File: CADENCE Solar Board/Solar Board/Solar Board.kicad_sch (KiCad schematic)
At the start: 52 parts, among them J1 Conn_01x08, U1 INA230AIRGTT, U2 AD7414ARTZ-1REEL7, U3 OPT3001IDNPRQ1

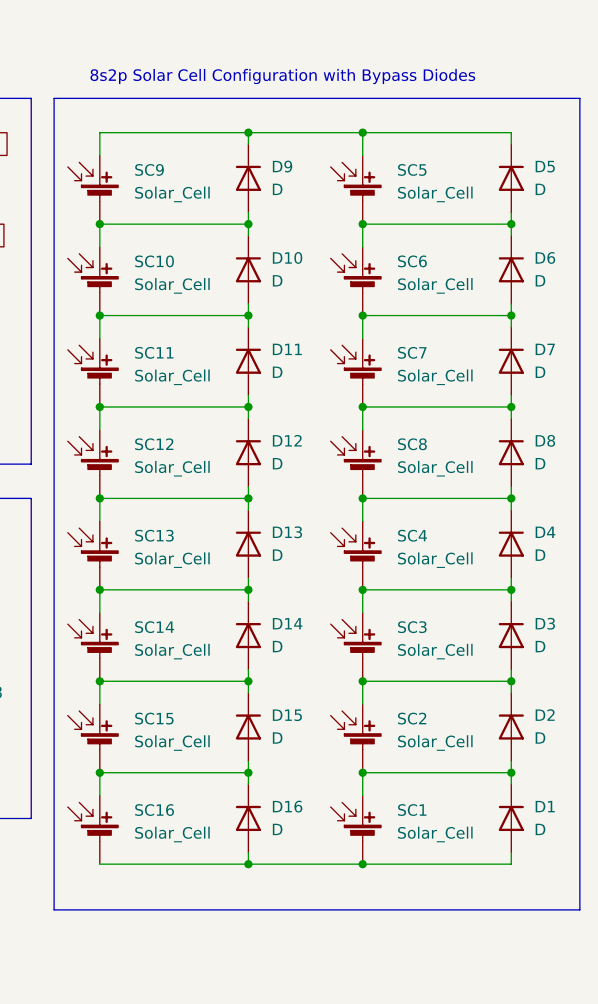
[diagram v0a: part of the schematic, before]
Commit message: added basic PCB layout and attached footprints to parts (excluding solar cells. a lot might need updating later)
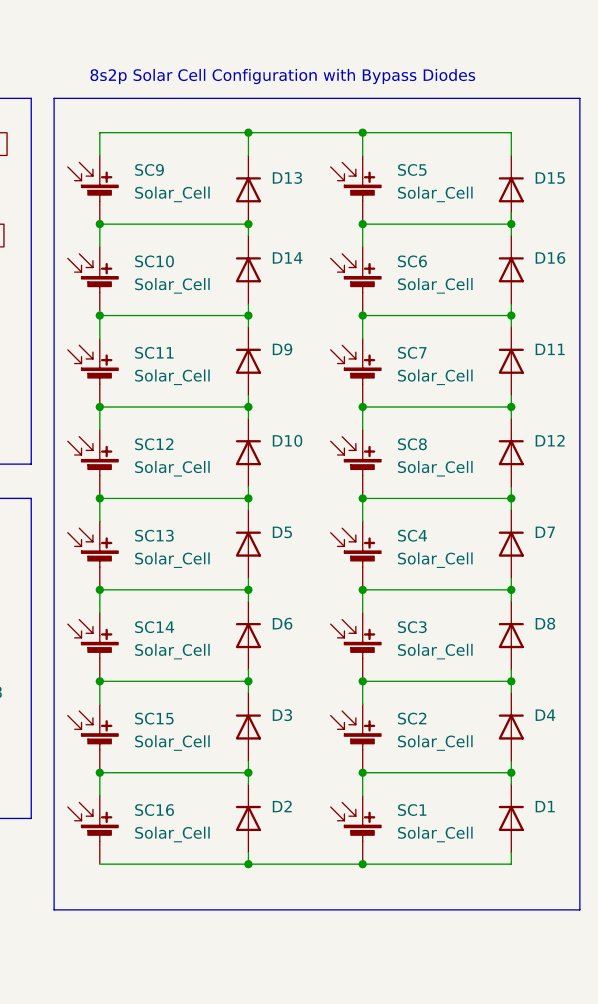
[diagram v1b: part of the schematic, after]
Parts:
- D1, D10, D11, D12, D13, D14, D15, D16, D2, D3, D4, D5, D6, D7, D8, D9: footprint (none) -> Diode_SMD:D_01005_0402Metric
- J1: footprint (none) -> Connector_PinHeader_1.00mm:PinHeader_1x08_P1.00mm_Horizontal
- R1, R10, R2, R3, R4, R5, R6, R7, R8, R9: footprint (none) -> Resistor_SMD:R_01005_0402Metric
- TP1, TP2, TP3: footprint (none) -> Connector_Pin:Pin_D1.3mm_L11.0mm_LooseFit
- U1: footprint QFN50P300X300X100-17N-D -> INA230AIRGTT:QFN50P300X300X100-17N-D
- U2: footprint SOT95P280X145-6N -> AD7414ARTZ-1REEL7:SOT95P280X145-6N
- U3: footprint SON65P200X200X65-7N-D -> OPT3001IDNPRQ1:SON65P200X200X65-7N-D
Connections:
- net at SC10.1 (+), SC9.2 (-): now also D13.2 (A), D14.1 (K); no longer D10.1 (K), D9.2 (A)
- net at SC10.2 (-), SC11.1 (+): now also D14.2 (A), D9.1 (K); no longer D10.2 (A), D11.1 (K)
- net at SC11.2 (-), SC12.1 (+): now also D10.1 (K), D9.2 (A); no longer D11.2 (A), D12.1 (K)
- net at SC12.2 (-), SC13.1 (+): now also D10.2 (A), D5.1 (K); no longer D12.2 (A), D13.1 (K)
- net at SC5.1 (+), SC9.1 (+): now also D13.1 (K), D15.1 (K); no longer D5.1 (K), D9.1 (K)
- net at SC6.2 (-), SC7.1 (+): now also D11.1 (K), D16.2 (A); no longer D6.2 (A), D7.1 (K)
- net at D7.2 (A), D8.1 (K): now also SC3.1 (+), SC4.2 (-); no longer SC7.2 (-), SC8.1 (+)
- net at SC13.2 (-), SC14.1 (+): now also D5.2 (A), D6.1 (K); no longer D13.2 (A), D14.1 (K)
- net at D1.1 (K), SC1.1 (+), SC2.2 (-): now also D4.2 (A); no longer D2.2 (A)
- net at D1.2 (A), SC1.2 (-), SC16.2 (-): now also D2.2 (A); no longer D16.2 (A)
- net at SC14.2 (-), SC15.1 (+): now also D3.1 (K), D6.2 (A); no longer D14.2 (A), D15.1 (K)
- net at SC15.2 (-), SC16.1 (+): now also D2.1 (K), D3.2 (A); no longer D15.2 (A), D16.1 (K)
- net at SC4.1 (+), SC8.2 (-): now also D12.2 (A), D7.1 (K); no longer D4.1 (K), D8.2 (A)
- net at SC2.1 (+), SC3.2 (-): now also D4.1 (K), D8.2 (A); no longer D2.1 (K), D3.2 (A)
- net at SC5.2 (-), SC6.1 (+): now also D15.2 (A), D16.1 (K); no longer D5.2 (A), D6.1 (K)
- new net: D11.2 (A), D12.1 (K), SC7.2 (-), SC8.1 (+)

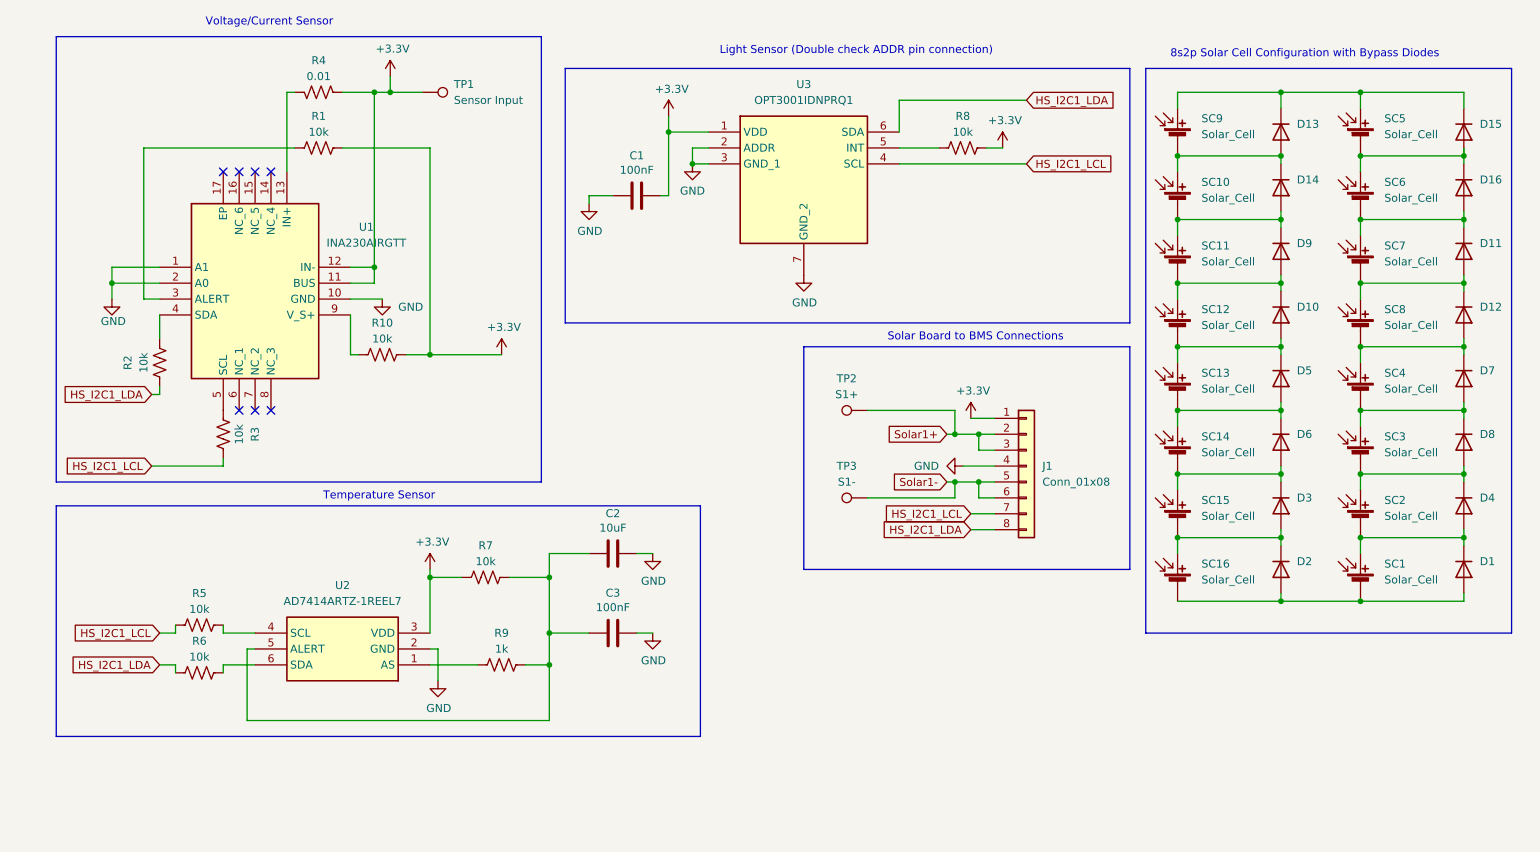
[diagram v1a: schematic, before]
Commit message: corrected board based on octavio's review
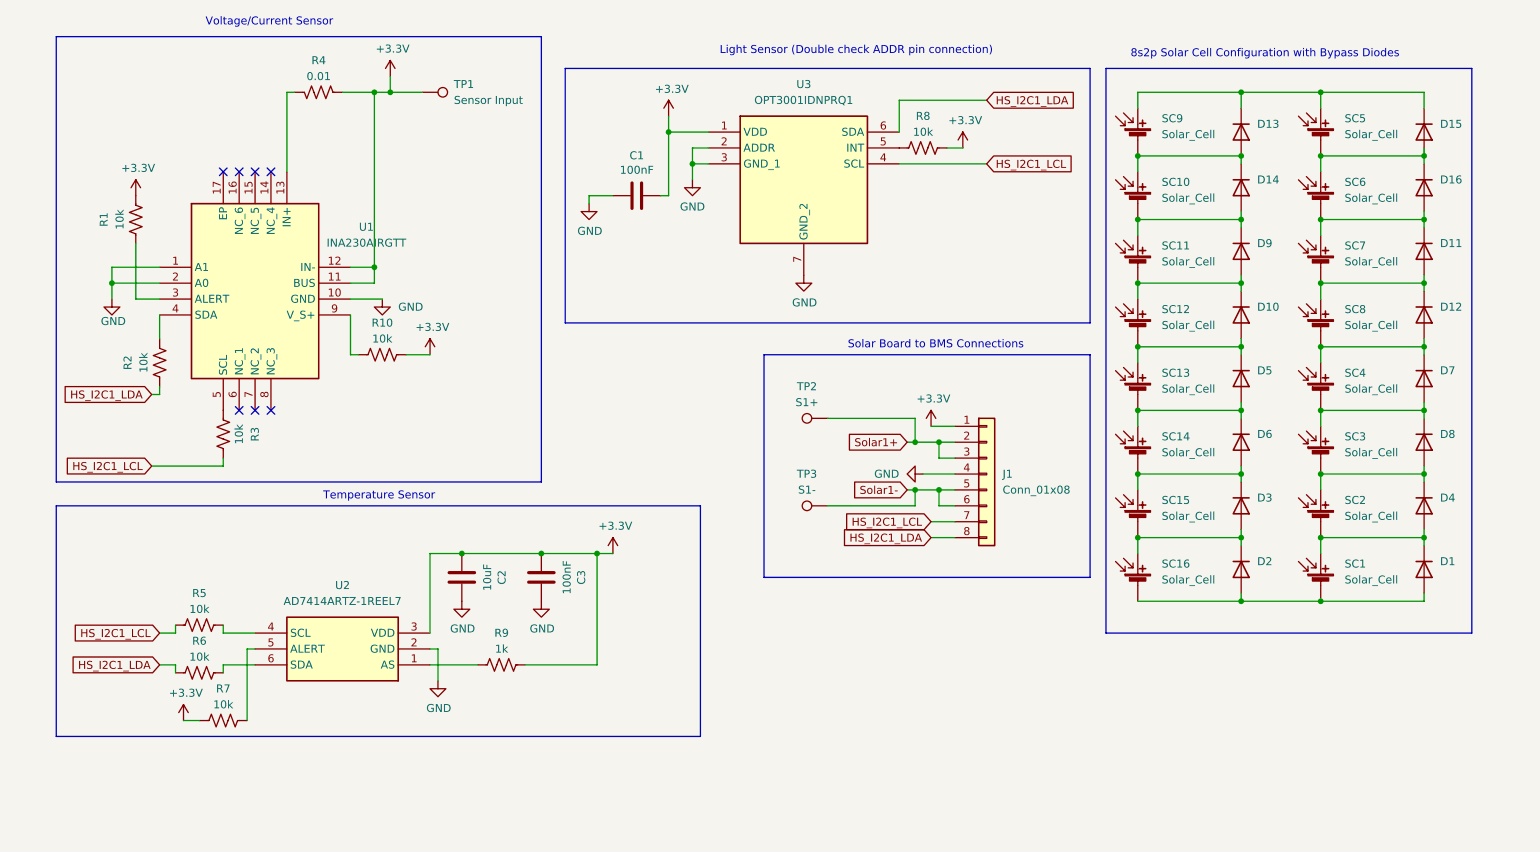
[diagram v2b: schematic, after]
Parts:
- R7: footprint Resistor_SMD:R_01005_0402Metric -> (none)
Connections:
- net +3.3V: now also C2.1, C3.1, R9.2
- new net: R7.2, U2.5 (ALERT)
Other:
- moved on the sheet: C2, C3, D1, D10, D11, D12, D13, D14, D15, D16, D2, D3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

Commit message: corrected board based on octavio's review
added led with resistor to ALERT pins, removed extra resistors, biased high configuration for the voltage/current sensor
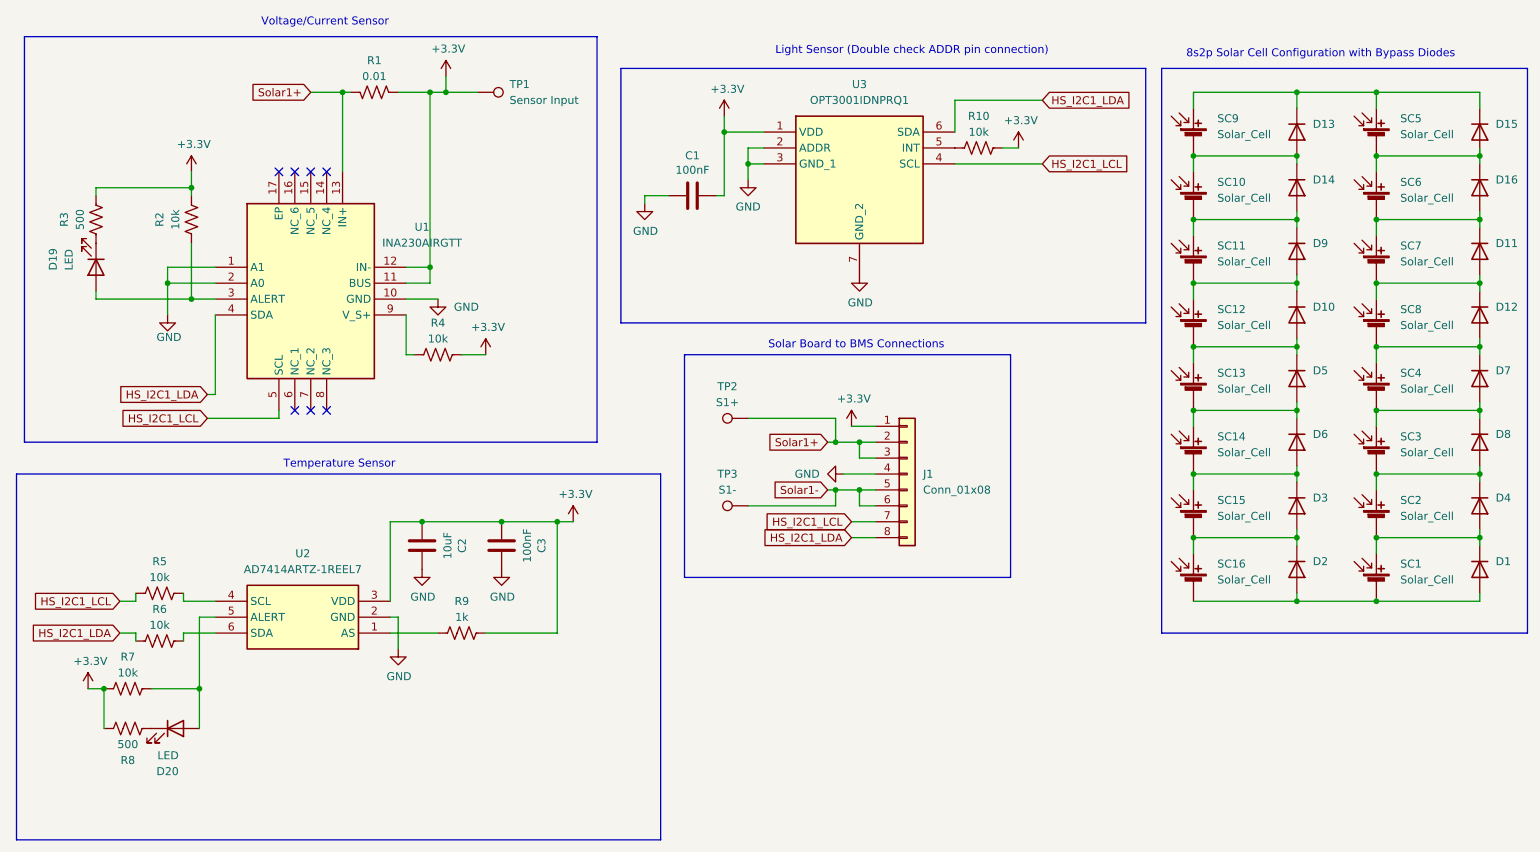
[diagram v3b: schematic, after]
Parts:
- removed R2: 10k, Resistor_SMD:R_01005_0402Metric, symbol Device:R_US
- added D19, D20: LED, symbol Device:LED
- added R8: 500, Resistor_SMD:R_01005_0402Metric, symbol Device:R_US
- R3: value 10k -> 500
- renumbered R4 to R1, R8 to R10, R1 to R2, R10 to R4
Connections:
- net +3.3V: now also R3.2, R8.2
- net HS_I2C1_LCL: now also U1.5 (SCL); no longer R3.2
- net HS_I2C1_LDA: now also U1.4 (SDA)
- net Solar1+: now also R1.2, U1.13 (IN+)
- net at R2.1, U1.3 (ALERT): now also D19.2 (A)
- net at R3.1: now also D19.1 (K); no longer U1.5 (SCL)
- net at R7.2, U2.5 (ALERT): now also D20.2 (A)
- new net: D20.1 (K), R8.1
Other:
- moved on the sheet: C1, C2, C3, D1, D10, D11, D12, D13, D14, D15, D16, D2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

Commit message: more fixes (diodes are placeholders)
removed extra resistors, corrected LEDs
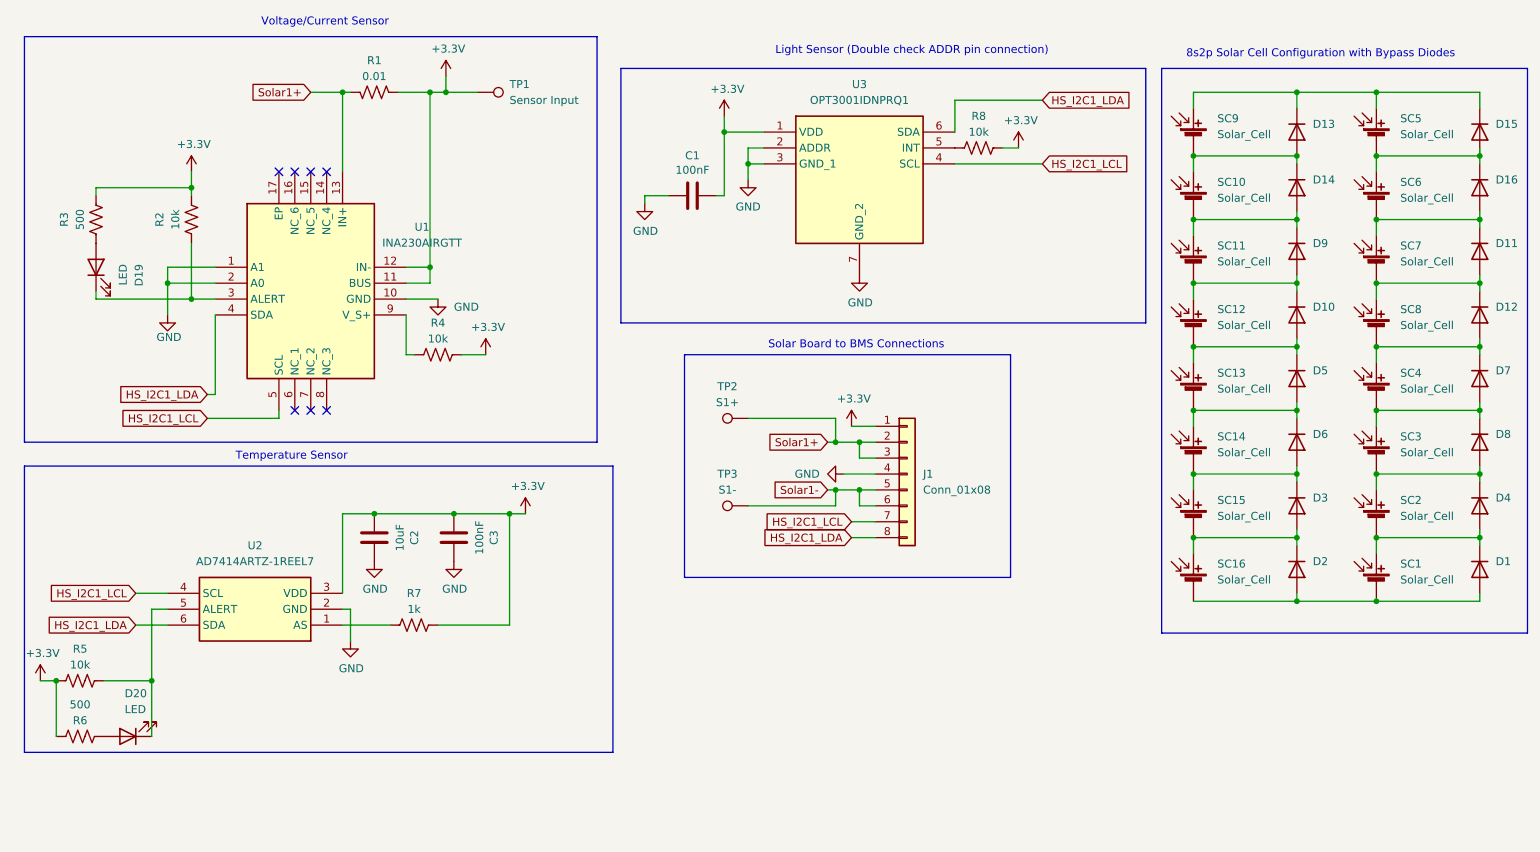
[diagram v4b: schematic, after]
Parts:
- removed R5, R6: 10k, Resistor_SMD:R_01005_0402Metric, symbol Device:R_US
- renumbered R7 to R5, R8 to R6, R9 to R7, R10 to R8
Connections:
- net HS_I2C1_LCL: now also U2.4 (SCL)
- net HS_I2C1_LDA: now also U2.6 (SDA)
- net at R2.1, U1.3 (ALERT): now also D19.1 (K); no longer D19.2 (A)
- net at R3.1: now also D19.2 (A); no longer D19.1 (K)
- net at R6.1: now also D20.2 (A); no longer D20.1 (K)
- net at R5.2, U2.5 (ALERT): now also D20.1 (K); no longer D20.2 (A)
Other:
- moved on the sheet: C2, C3, D19, D20, R5, R6, R7, U2

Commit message: fixed LEDs and reduced amount of bypass diodes by half
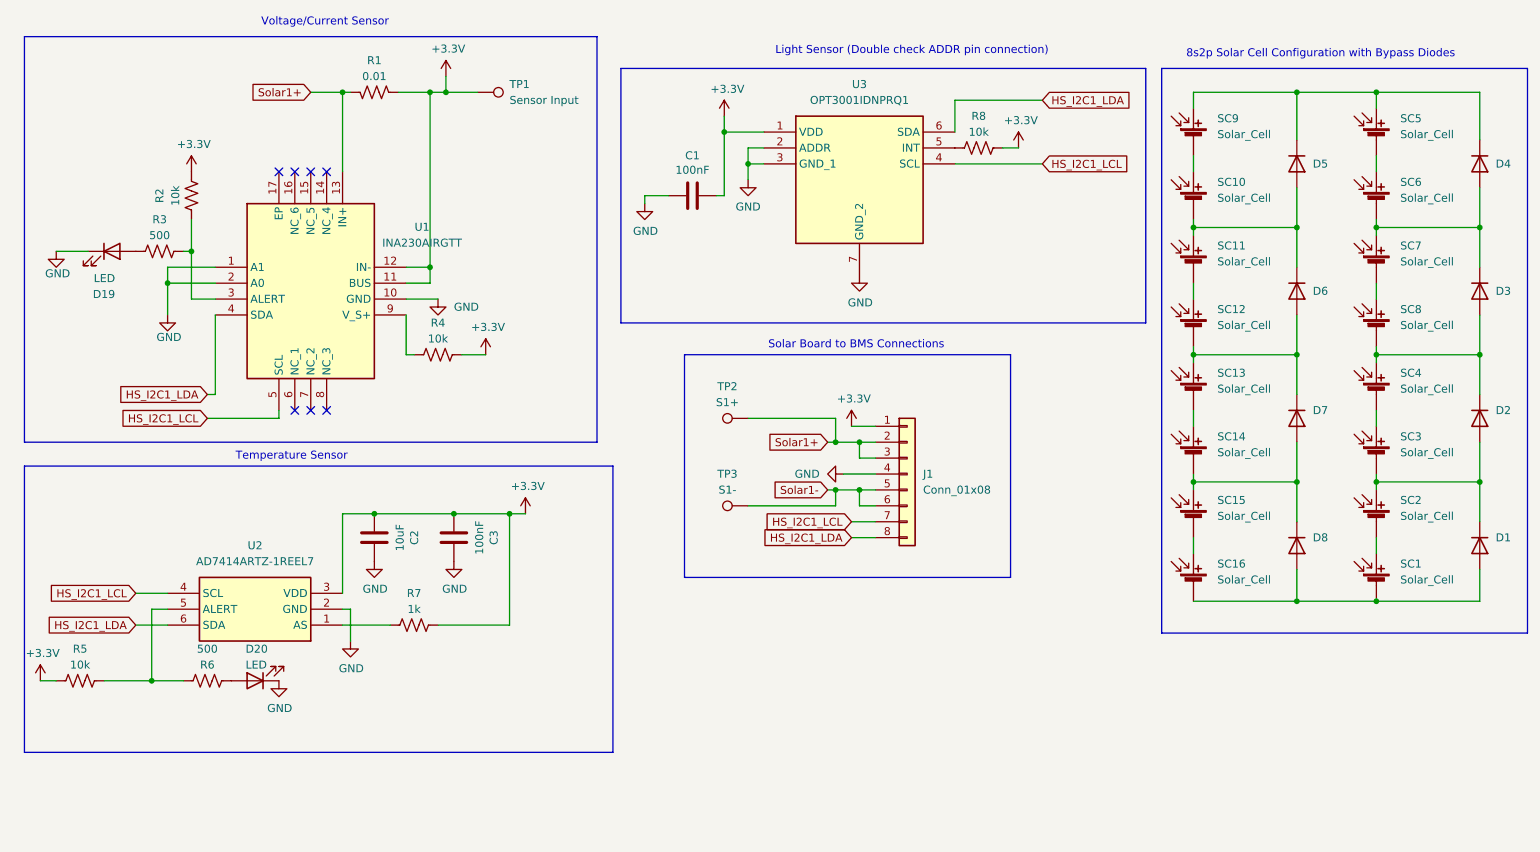
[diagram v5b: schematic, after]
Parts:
- removed D10, D11, D12, D13, D14, D15, D16, D9: D, Diode_SMD:D_01005_0402Metric, symbol Device:D
- D1, D2, D3, D4, D5, D6, D7, D8: footprint Diode_SMD:D_01005_0402Metric -> SK44BL-TP:DIOM4336X265N
- J1: footprint Connector_PinHeader_1.00mm:PinHeader_1x08_P1.00mm_Horizontal -> Connector_JST:JST_XH_B8B-XH-A_1x08_P2.50mm_Vertical
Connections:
- net +3.3V: no longer R3.2, R6.2
- net GND: now also D19.1 (K), D20.1 (K)
- net at SC10.2 (-), SC11.1 (+): now also D5.2 (A), D6.1 (K)
- net at SC12.2 (-), SC13.1 (+): now also D6.2 (A), D7.1 (K); no longer D5.1 (K)
- net at SC4.1 (+), SC8.2 (-): now also D2.1 (K), D3.2 (A); no longer D7.1 (K)
- net at D7.2 (A), D8.1 (K): now also SC14.2 (-), SC15.1 (+); no longer SC3.1 (+), SC4.2 (-)
- net at R2.1, U1.3 (ALERT): now also R3.2; no longer D19.1 (K)
- net at SC13.2 (-), SC14.1 (+): no longer D5.2 (A), D6.1 (K)
- net at SC15.2 (-), SC16.1 (+): no longer D2.1 (K), D3.2 (A)
- net at SC5.1 (+), SC9.1 (+): now also D4.1 (K), D5.1 (K)
- net at SC2.1 (+), SC3.2 (-): now also D1.1 (K), D2.2 (A); no longer D4.1 (K), D8.2 (A)
- net at SC1.1 (+), SC2.2 (-): no longer D1.1 (K), D4.2 (A)
- net at SC6.2 (-), SC7.1 (+): now also D3.1 (K), D4.2 (A)
- net at D1.2 (A), SC1.2 (-), SC16.2 (-): now also D8.2 (A); no longer D2.2 (A)
- net at R5.2, U2.5 (ALERT): now also R6.2; no longer D20.1 (K)
- new net: SC3.1 (+), SC4.2 (-)
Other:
- moved on the sheet: D1, D19, D20, R2, R3, R6
